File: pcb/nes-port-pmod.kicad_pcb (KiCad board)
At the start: 2 copper layers, 38.1 x 31.8 mm, 2 parts, among them J1 Conn_02x06_Top_Bottom, J2 NES_Port_Male

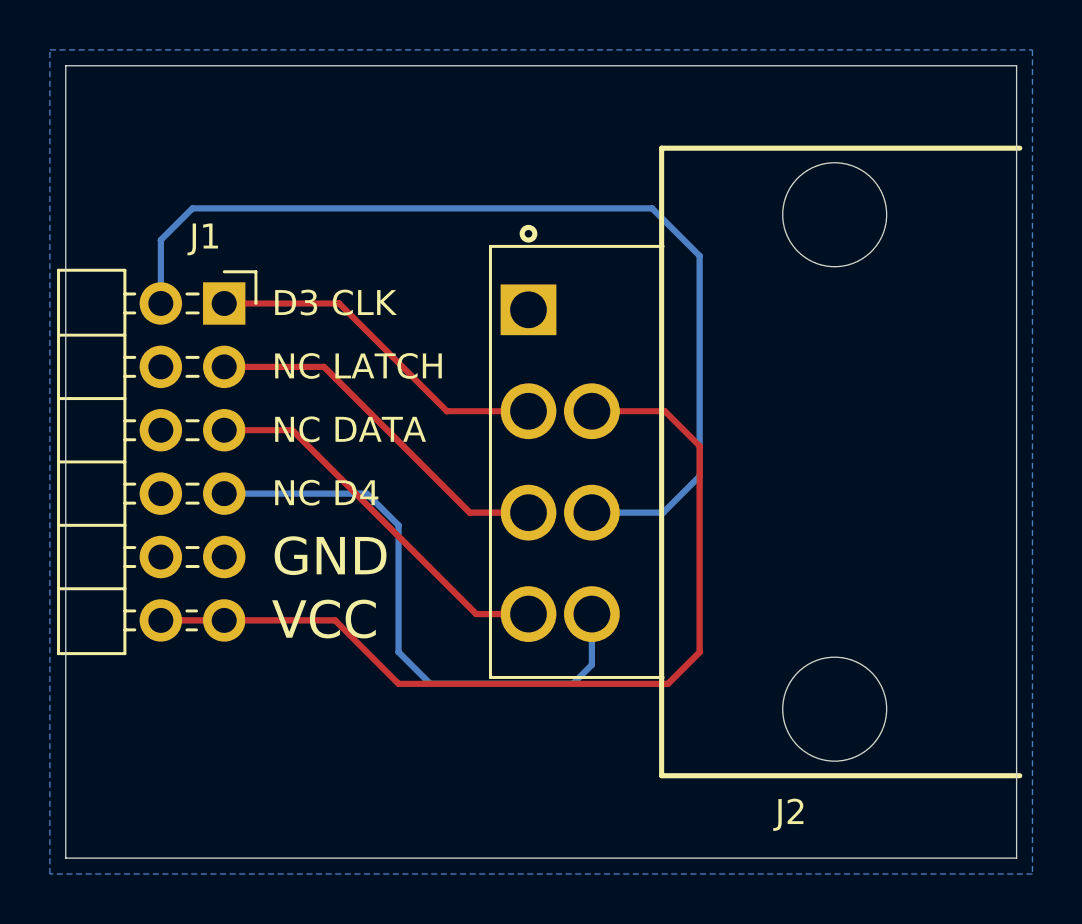
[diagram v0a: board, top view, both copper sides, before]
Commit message: Tweak Pmod pin header
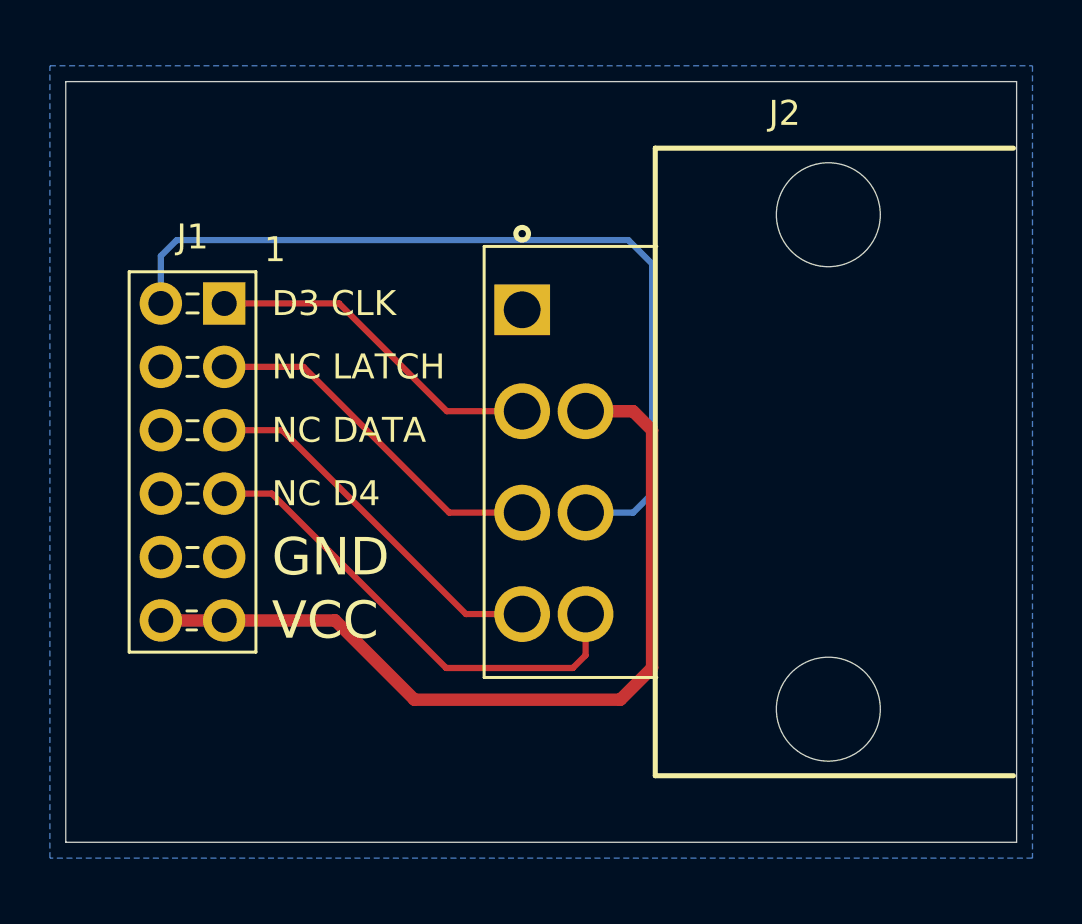
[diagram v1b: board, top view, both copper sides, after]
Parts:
- moved J2 0.25 mm to (125.5, 94.6)
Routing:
- net /D3: track 39.2 -> 34.4 mm
- net /D4: track 23.7 -> 19.2 mm
- net /VCC: track 36.3 -> 34.0 mm
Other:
- board size 38.1 x 31.8 mm -> 38.1 x 30.5 mm
- net class Power added: clearance 0.2, trace_width 0.5, via_dia 0.8, via_drill 0.4

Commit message: Update design rules and net classes. Update traces to match.
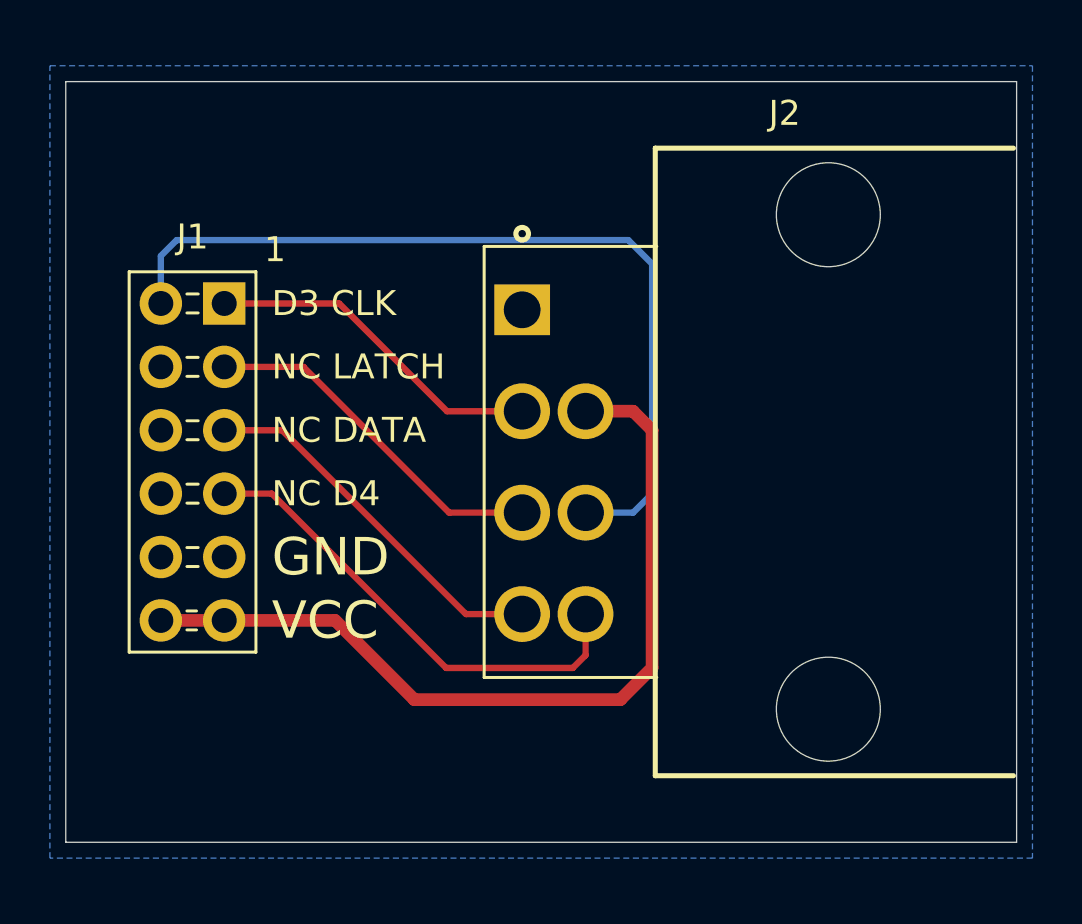
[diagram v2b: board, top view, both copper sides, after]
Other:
- net class Default: clearance 0.2 -> 0.254; trace_width 0.25 -> 0.254; via_dia 0.8 -> 0.762; via_drill 0.4 -> 0.381
- net class Power: clearance 0.2 -> 0.254; trace_width 0.5 -> 0.508; via_dia 0.8 -> 0.762; via_drill 0.4 -> 0.381
- rule pad_to_mask_clearance: 0 -> 0.0508
- rule trace_clearance: 0.2 -> 0.254
- rule trace_min: 0.2 -> 0.1524
- rule via_min_drill: 0.3 -> 0.254
- rule via_min_size: 0.4 -> 0.127

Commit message: Tweak PCB silkscreen
Add page info
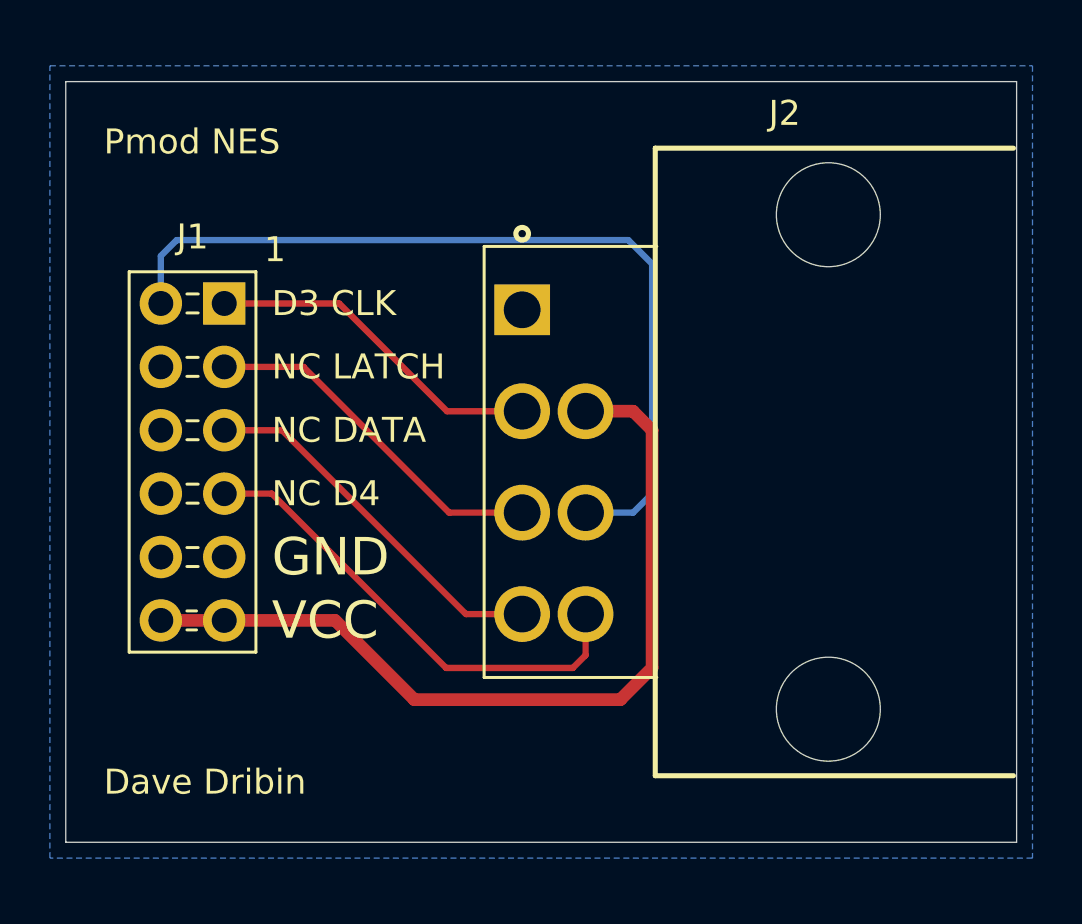
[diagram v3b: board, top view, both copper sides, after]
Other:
- board text added: "Dave Dribin"
- board text added: "Pmod NES"
- board text added: "Ver. 1.0"
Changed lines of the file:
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@@
   (general
     (thickness 1.6)
-    (drawings 12)
+    (drawings 15)
     (tracks 29)
     (zones 0)
@@
     (nets 11)
   )
-  (page A4)
+  (page USLetter)
+  (title_block
+    (title "NES Port Pmod Adapter")
+    (date 2021-08-01)
+    (rev 1.0)
+    (comment 3 "MIT License")
+    (comment 4 "Author: Dave Dribin")
+  )
   (layers
     (0 F.Cu signal)
@@
       (padsonsilk false)
       (subtractmaskfromsilk false)
-      (outputformat 1)
+      (outputformat 4)
       (mirror false)
-      (drillshape 1)
+      (drillshape 0)
       (scaleselection 1)
-      (outputdirectory ""))
+      (outputdirectory "pdf"))
   )
   (net 0 "")
@@
     (add_net /D4)
     (add_net /DATA)
-    (add_net /GND)
     (add_net /LATCH)
     (add_net "Net-(J1-Pad10)")
@@
     (uvia_dia 0.762)
     (uvia_drill 0.381)
+    (add_net /GND)
     (add_net /VCC)
   )
@@
     )
   )
+  (gr_text "Ver. 1.0" (at 109.474 81.788) (layer B.SilkS)
+    (effects (font (size 1 1) (thickness 0.15)) (justify right mirror))
+  )
+  (gr_text "Pmod NES" (at 109.474 81.788) (layer F.SilkS)
+    (effects (font (size 1 1) (thickness 0.15)) (justify left))
+  )
+  (gr_text "Dave Dribin" (at 109.474 107.442) (layer F.SilkS)
+    (effects (font (size 1 1) (thickness 0.15)) (justify left))
+  )
   (gr_text "D3 CLK" (at 116.205 88.265) (layer F.SilkS)
